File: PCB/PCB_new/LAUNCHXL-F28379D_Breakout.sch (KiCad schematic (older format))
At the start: 25 parts, among them IC1 LM358N, Q1 220mA/50V/3.5Ω, Q10 100V/17A, Q2 100V/17A, Q6 100V/17A, Q7 100V/17A, Q8 100V/17A, Q9 100V/17A

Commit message: updated schematic and packages (need to verify many packages)
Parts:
- removed BRAKE_CONN: 1X2-3.5MM, Drivetrain_control:1X2-3.5MM, symbol PCB_2020-rescue:1X2-3.5MM-Drivetrain_control-eagle-import-Board_Schematic_11201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
- removed D1: 1N4004, Drivetrain_control:DO41-10, symbol PCB_2020-rescue:1N4004-Drivetrain_control-eagle-import-Board_Schematic_112019-r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
- removed unit 2 of DCDC_CONN_12V
- removed unit 2 of IC1
- removed unit 2 of JETSON_CONN_PWR
- removed unit 3 of JETSON_CONN_PWR
- removed MC_CONN: 22-23-2041, Drivetrain_control:22-23-2041, symbol PCB_2020-rescue:22-23-2041-Drivetrain_control-eagle-import-Board_Schematic_1120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
- removed Q10, Q6, Q7, Q8, Q9: 100V/17A, Drivetrain_control:TO220V, symbol PCB_2020-rescue:MOSFET-NCH-FQP30N06L-Drivetrain_control-eagle-import-Board_Sche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
- removed R9: R-US_R0805, Drivetrain_control:R0805, symbol PCB_2020-rescue:R-US_R0805-Drivetrain_control-eagle-import-Board_Schematic_1120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
- removed SERVO_CONN: 5566-8, Drivetrain_control:5566-8, symbol PCB_2020-rescue:5566-8-Drivetrain_control-eagle-import-Board_Schematic_112019-r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
- added J?: SERVO_CONN, symbol Connector:Conn_01x08_Male
- added J?: MC_CONN, Connector_Molex:Molex_Mini-Fit_Jr_5566-04A2_2x02_P4.20mm_Vertical, symbol Connector:Conn_01x04_Male
- added Q? (x4): 100V/17A, Package_TO_SOT_THT:TO-251-3_Vertical, symbol Device:Q_NMOS_DGS
- C1: symbol PCB_2020-rescue:C-Drivetrain_control-eagle-import-Board_Schematic_112019-rescue-PCB_2020-rescue-PCB_2020-rescue -> Device:C
- DCDC_CONN_12V: footprint Drivetrain_control:22-23-2021 -> Connector_Molex:Molex_CLIK-Mate_502382-0270_1x02-1MP_P1.25mm_Vertical; symbol PCB_2020-rescue:22-23-2021-Drivetrain_control-eagle-import-Board_Schematic_112019-rescue-PCB_2020-rescue-PCB_2020-rescue -> Connector:Conn_01x02_Male
- FTDI: symbol PCB_2020-rescue:CONN_06LONGPADS-Drivetrain_control-eagle-import-Board_Schematic_112019-rescue-PCB_2020-rescue-PCB_2020-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 -> PCB_2020:CONN_06LONGPADS-Drivetrain_control
- IC1: footprint Drivetrain_control:DIL08 -> Package_DIP:DIP-8_W10.16mm; symbol PCB_2020-rescue:LM358N-Drivetrain_control-eagle-import-Board_Schematic_112019-rescue-PCB_2020-rescue-PCB_2020-rescue -> Amplifier_Operational:LM358
- JETSON_CONN_PWR: footprint Drivetrain_control:22-23-2031 -> Connector_Molex:Molex_CLIK-Mate_502382-0370_1x03-1MP_P1.25mm_Vertical; symbol PCB_2020-rescue:22-23-2031-Drivetrain_control-eagle-import-Board_Schematic_112019-rescue-PCB_2020-rescue-PCB_2020-rescue -> Connector:Conn_01x03_Male
- Q1: footprint Drivetrain_control:SOT23-3 -> Package_TO_SOT_THT:TO-251-3_Vertical; symbol PCB_2020-rescue:MOSFET-NCH-BSS138-Drivetrain_control-eagle-import-Board_Schematic_112019-rescue-PCB_2020-rescue-PCB_202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 -> Device:Q_NMOS_DGS
- Q2: footprint Drivetrain_control:TO220V -> Package_TO_SOT_THT:TO-251-3_Vertical; symbol PCB_2020-rescue:MOSFET-NCH-FQP30N06L-Drivetrain_control-eagle-import-Board_Schematic_112019-rescue-PCB_2020-rescue-PCB_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 -> Device:Q_NMOS_DGS
- R1, R18, R2, R3, R4, R5: symbol PCB_2020-rescue:R-US_R0805-Drivetrain_control-eagle-import-Board_Schematic_112019-rescue-PCB_2020-rescue-PCB_2020-rescue -> Device:R
- R16, R17: footprint Drivetrain_control:R0805 -> Resistor_SMD:R_0805_2012Metric_Pad1.15x1.40mm_HandSolder; symbol PCB_2020-rescue:R-US_R0805-Drivetrain_control-eagle-import-Board_Schematic_112019-rescue-PCB_2020-rescue-PCB_2020-rescue -> Device:R
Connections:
- net +12V: now also DCDC_CONN_12V.2 (Pin_2), R18.1, R2.1, R5.1; no longer DCDC_CONN_12V.1 (S), IC1.8 (V+), R18.2, R2.2, R5.2
- net +3V3: now also JETSON_CONN_PWR.2 (Pin_2), Q1.2 (G), R1.1; no longer Q1.1 (G), R1.2
- net +5V: now also JETSON_CONN_PWR.3 (Pin_3); no longer JETSON_CONN_PWR.1 (S)
- net EN+: now also R5.2, J?.5 (Pin_5), Q?.1 (D); no longer R5.1
- net EN+_CTL: now also Q?.2 (G)
- net FS1_CTL: now also Q?.2 (G)
- net FS1_MC: now also J?.4 (Pin_4), Q?.1 (D)
- net FWD_CTL: now also Q?.2 (G)
- net FWD_MC: now also J?.3 (Pin_3), Q?.1 (D)
- net GND: now also DCDC_CONN_12V.1 (Pin_1), JETSON_CONN_PWR.1 (Pin_1), R17.2, R3.2, J?.1 (Pin_1), J?.2 (Pin_2), J?.3 (Pin_3), J?.4 (Pin_4), Q?.3 (S), Q?.3 (S), Q?.3 (S), Q?.3 (S); no longer IC1.4 (V-), R17.1, R3.1
- net HLFB+: now also R16.1, J?.8 (Pin_8); no longer R16.2
- net INPUT_A+: now also Q2.1 (D), R18.2, J?.6 (Pin_6); no longer Q2.2 (D), R18.1
- net INPUT_A+_CTL: now also Q2.2 (G); no longer Q2.1 (G)
- net INPUT_B+: now also Q1.1 (D), R2.2, J?.7 (Pin_7); no longer Q1.3 (D), R2.1
- net MC_HLFB+: now also R16.2, R17.1; no longer R16.1, R17.2
- net REV_CTL: now also Q?.2 (G)
- net REV_MC: now also J?.2 (Pin_2), Q?.1 (D)
- net THROTTLE_DAC: now also IC1.3 (+)
- net THROTTLE_MC: now also IC1.1, R4.2, J?.1 (Pin_1); no longer R4.1
- net TI_PWM: now also Q1.3 (S), R1.2; no longer Q1.2 (S), R1.1
- new net: IC1.2 (-), R3.1, R4.1
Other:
- note added: "Check to make sure that the mollex connection is correct for these!!"
- note added: "Info from past connector\nDrivetrain_control:22-23-2041\nPCB_2020-rescue:22-23-2041-Drivetrain_control-eagle-import"
- note added: "check size of molex connector"
- note added: "check this mollex connector too!!"
- note added: "find out what happened to the ground Vdd pins\n"

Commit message: cleaned up breakout and headers files
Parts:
- IC1: symbol Amplifier_Operational:LM358 -> PCB_2020:LM358_with_power_pins
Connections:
- net +12V: now also IC1.5
- net GND: now also IC1.4
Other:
- note removed: "find out what happened to the ground Vdd pins\n"
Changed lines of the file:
@@
 EESchema Schematic File Version 4
+LIBS:PCB_2020-cache
 EELAYER 30 0
 EELAYER END
@@
 encoding utf-8
 Sheet 3 3
-Title ""
-Date ""
+Title "AMP Breakout"
+Date "2019-12-13"
 Rev ""
 Comp ""
@@
 Wire Wire Line
 	3100 3800 3100 4000
-Text GLabel 2600 3800 2    70   BiDi ~ 0
-GND
-Wire Wire Line
-	4600 3800 4600 3900
 Wire Wire Line
 	4600 3900 5300 3900
@@
 	7400 1500 7200 1500
 Wire Wire Line
-	2300 1500 2300 1600
-Wire Wire Line
-	2300 1600 2300 1700
-Wire Wire Line
-	2300 1700 2300 1800
-Wire Wire Line
-	3000 1600 2300 1600
-Text GLabel 2700 1500 2    70   BiDi ~ 0
-GND
-Text GLabel 2700 1600 2    70   BiDi ~ 0
-GND
-Connection ~ 2300 1600
-Text GLabel 2700 1700 2    70   BiDi ~ 0
-GND
-Connection ~ 2300 1700
-Text GLabel 2700 1800 2    70   BiDi ~ 0
-GND
-Connection ~ 2300 1800
-Wire Wire Line
 	7800 3400 7800 3500
 Wire Wire Line
 	10300 1700 10200 1700
 Wire Wire Line
-	4900 3500 5100 3500
-Wire Wire Line
 	5100 3500 5100 4100
 Wire Wire Line
 	5100 3500 5600 3500
-Connection ~ 5100 3500
 Text Label 5450 3500 0    70   ~ 0
 THROTTLE_MC
-Text Label 10950 4650 2    70   ~ 0
+Text Label 10950 4650 2    39   ~ 0
 THROTTLE_MC
 Wire Wire Line
 	4300 3600 4300 4100
 Connection ~ 4300 4100
-Wire Wire Line
-	4300 3400 4100 3400
-Text GLabel 4100 3400 0    70   BiDi ~ 0
+Text GLabel 4100 3400 0    39   BiDi ~ 0
 THROTTLE_DAC
 Wire Wire Line
 	2000 3400 2600 3400
-Text GLabel 2600 3400 2    70   BiDi ~ 0
+Text GLabel 2600 3400 2    39   BiDi ~ 0
 SCIB_RX
 Wire Wire Line
 	2000 3500 2600 3500
-Text GLabel 2600 3500 2    70   BiDi ~ 0
+Text GLabel 2600 3500 2    39   BiDi ~ 0
 SCIB_TX
 Wire Wire Line
@@
 Wire Wire Line
 	3100 3600 3100 3000
-Text GLabel 2600 3600 2    70   BiDi ~ 0
-+3V3
 Wire Wire Line
 	4800 1300 4800 1100
@@
 Wire Wire Line
 	9800 1600 9800 1300
-Wire Wire Line
-	4600 3200 4600 2900
 Wire Wire Line
 	4600 2900 4600 2700
@@
 Wire Wire Line
 	3000 1400 2900 1400
-Text Label 2900 1400 2    70   ~ 0
+Text Label 2900 1400 2    39   ~ 0
 EN+
 Wire Wire Line
@@
 Wire Wire Line
 	3000 1300 2900 1300
-Text Label 2900 1300 2    70   ~ 0
+Text Label 2900 1300 2    39   ~ 0
 INPUT_A+
 Wire Wire Line
@@
 Wire Wire Line
 	1900 1100 1900 1400
-Text Label 1900 1100 0    70   ~ 0
+Text Label 1900 1100 0    39   ~ 0
 HLFB+
 Wire Wire Line
@@
 Text Label 11100 2900 0    70   ~ 0
 FS1_MC
-Text Label 10950 4350 2    70   ~ 0
+Text Label 10950 4350 2    39   ~ 0
 FS1_MC
 Wire Wire Line
@@
 Text Label 8900 2900 0    70   ~ 0
 REV_MC
-Text Label 10950 4550 2    70   ~ 0
+Text Label 10950 4550 2    39   ~ 0
 REV_MC
 Text Label 4500 1700 2    70   ~ 0
@@
 Wire Wire Line
 	10200 1500 10200 1300
-Text GLabel 8600 3200 3    70   BiDi ~ 0
+Text GLabel 8600 3200 3    39   BiDi ~ 0
 REV_CTL
-Text GLabel 6400 3200 3    70   BiDi ~ 0
+Text GLabel 6400 3200 3    39   BiDi ~ 0
 EN+_CTL
-Text GLabel 9700 3200 3    70   BiDi ~ 0
+Text GLabel 9700 3200 3    39   BiDi ~ 0
 FWD_CTL
-Text GLabel 10800 3200 3    70   BiDi ~ 0
+Text GLabel 10800 3200 3    39   BiDi ~ 0
 FS1_CTL
-Text GLabel 1900 1800 0    70   BiDi ~ 0
+Text GLabel 1900 1800 0    39   BiDi ~ 0
 MC_HLFB+
-Text GLabel 7500 3200 3    70   BiDi ~ 0
+Text GLabel 7500 3200 3    39   BiDi ~ 0
 INPUT_A+_CTL
 $Comp
@@
 $EndComp
 $Comp
-L Amplifier_Operational:LM358 IC1
+L PCB_2020:LM358_with_power_pins IC1
 U 1 1 70C115B9
-P 4600 3500
+P 4650 3500
 AR Path="/70C115B9" Ref="IC1"  Part="3"
 AR Path="/5DD5E236/70C115B9" Ref="IC1"  Part="3"
 AR Path="/5DF27AC1/70C115B9" Ref="IC1"  Part="1"
-F 0 "IC1" H 4700 3625 59  0001 L BNN
-F 1 "LM358N" H 4700 3300 59  0001 L BNN
-F 2 "Package_DIP:DIP-8_W10.16mm" H 4600 3500 50  0001 C CNN
-F 3 "" H 4600 3500 50  0001 C CNN
-	1    4600 3500
+F 0 "IC1" H 4750 3625 59  0001 L BNN
+F 1 "LM358N" H 4750 3300 59  0001 L BNN
+F 2 "Package_DIP:DIP-8_W10.16mm" H 4650 3500 50  0001 C CNN
+F 3 "" H 4650 3500 50  0001 C CNN
+	1    4650 3500
 	1    0    0    -1
 $EndComp
@@
 L power:GND #GND16
 U 1 1 4CC6CA08
-P 2300 2100
+P 2650 2100
 AR Path="/4CC6CA08" Ref="#GND16"  Part="1"
 AR Path="/5DD5E236/4CC6CA08" Ref="#GND16"  Part="1"
 AR Path="/5DF27AC1/4CC6CA08" Ref="#GND16"  Part="1"
-F 0 "#GND16" H 2300 2100 50  0001 C CNN
-F 1 "GND" H 2200 1900 59  0000 L BNN
-F 2 "" H 2300 2100 50  0001 C CNN
-F 3 "" H 2300 2100 50  0001 C CNN
-	1    2300 2100
+F 0 "#GND16" H 2650 2100 50  0001 C CNN
+F 1 "GND" H 2550 1900 59  0000 L BNN
+F 2 "" H 2650 2100 50  0001 C CNN
+F 3 "" H 2650 2100 50  0001 C CNN
+	1    2650 2100
 	1    0    0    -1
 $EndComp
@@
 Text Notes 7200 900  0    59   ~ 0
 12V supply comes from DC-DC Converter\nwhich supplies 13.8 nominal and 12V @ peak current
-Wire Wire Line
-	2300 1500 3000 1500
 Text GLabel 4800 1700 3    50   Input ~ 0
 TI_PWM
@@
 Wire Wire Line
 	1900 2250 1900 2500
-Wire Wire Line
-	2300 1800 2300 2100
-Text Label 2900 1200 2    70   ~ 0
+Text Label 2900 1200 2    39   ~ 0
 INPUT_B+
 $Comp
@@
 Text Notes 2250 750  0    50   ~ 10
 check size of molex connector
-Wire Wire Line
-	3000 1800 2300 1800
-Wire Wire Line
-	3000 1700 2300 1700
 $Comp
 L Connector:Conn_01x08_Male J?
@@
 Text Notes 10900 4950 0    50   ~ 10
 Info from past connector\nDrivetrain_control:22-23-2041\nPCB_2020-rescue:22-23-2041-Drivetrain_control-eagle-import
-Text Label 10950 4450 2    70   ~ 0
+Text Label 10950 4450 2    39   ~ 0
 FWD_MC
 Wire Wire Line
@@
 Wire Wire Line
 	5300 3250 5300 3900
-Text Notes 4100 2900 0    50   ~ 10
-find out what happened to the ground Vdd pins\n
+Wire Wire Line
+	4100 3400 4350 3400
+Wire Wire Line
+	4300 3600 4350 3600
+Wire Wire Line
+	4600 3750 4600 3900
+Wire Wire Line
+	4600 2900 4600 3250
+Wire Wire Line
+	4950 3500 5100 3500
+Connection ~ 5100 3500
+Wire Wire Line
+	2650 1500 2650 1600
+Wire Wire Line
+	3000 1500 2650 1500
+Wire Wire Line
+	3000 1600 2650 1600
+Connection ~ 2650 1600
+Wire Wire Line
+	2650 1600 2650 1700
+Wire Wire Line
+	3000 1700 2650 1700
+Connection ~ 2650 1700
+Wire Wire Line
+	3000 1800 2650 1800
+Wire Wire Line
+	2650 1700 2650 1800
+Connection ~ 2650 1800
+Wire Wire Line
+	2650 1800 2650 2100
 $EndSCHEMATC

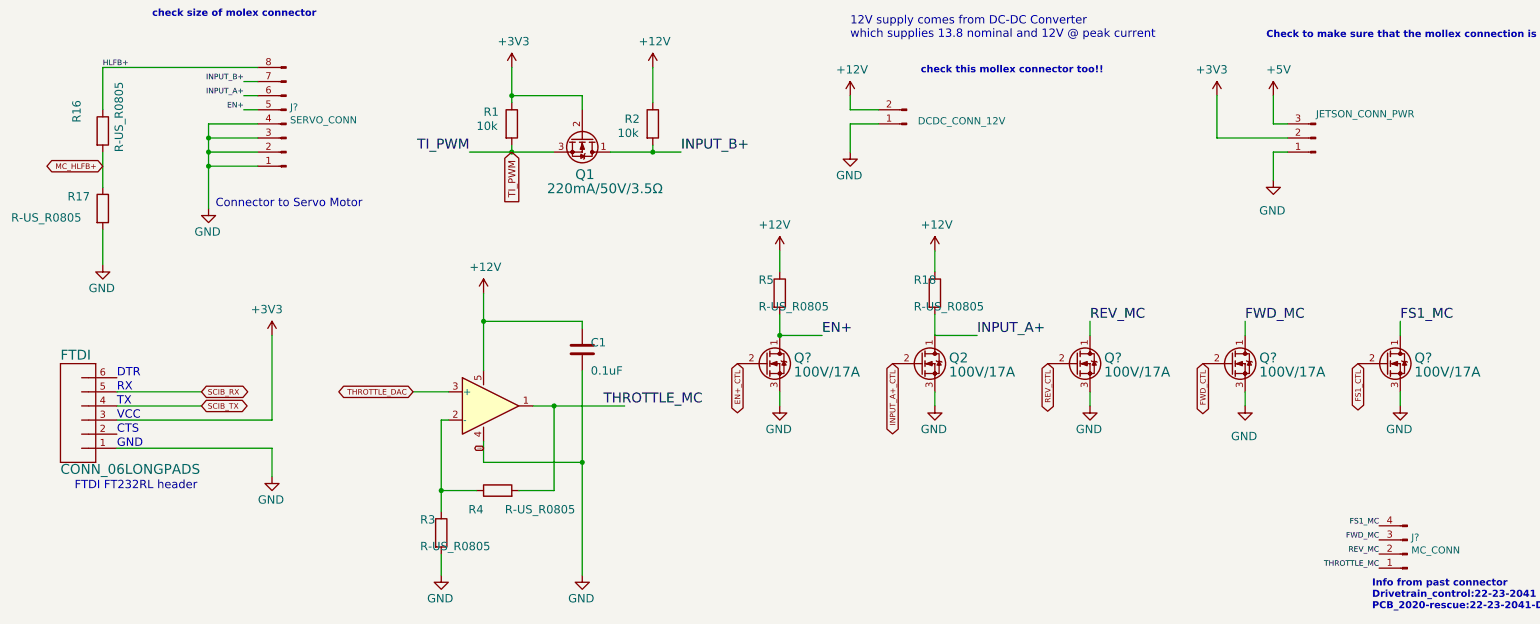
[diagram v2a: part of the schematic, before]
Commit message: added no connection indicators
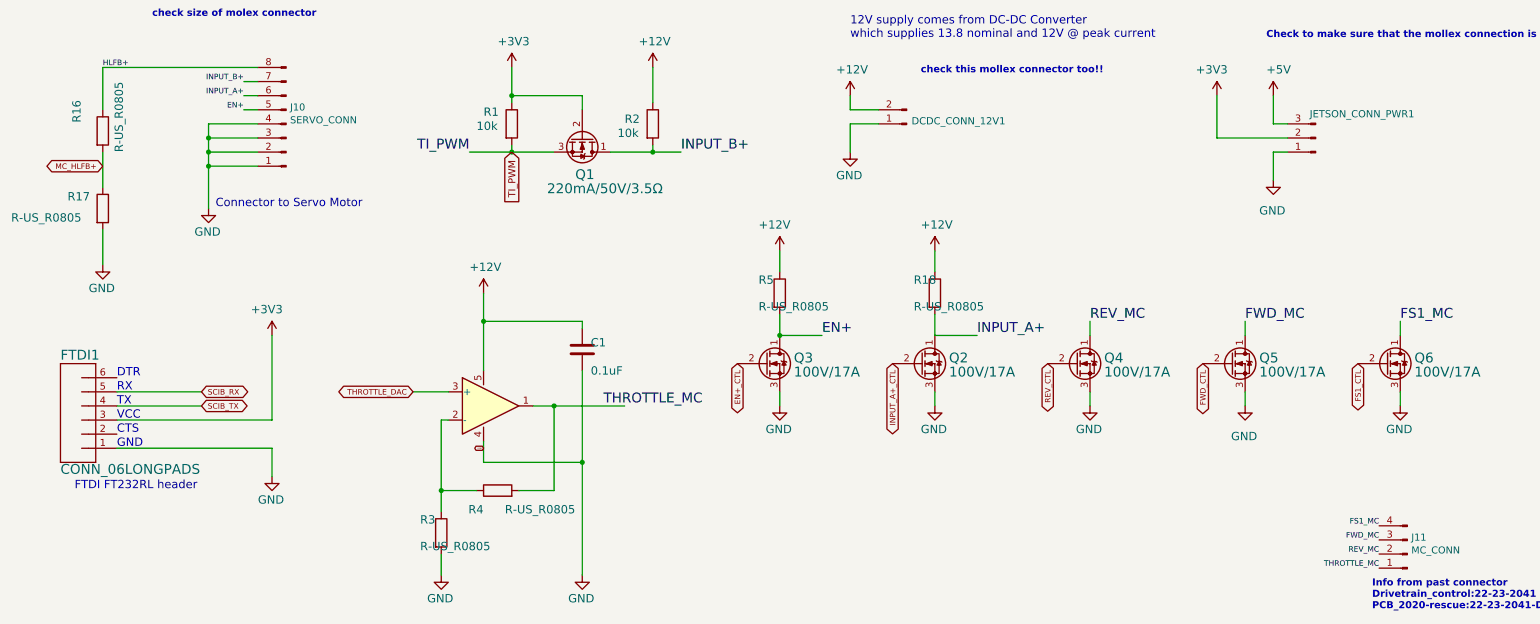
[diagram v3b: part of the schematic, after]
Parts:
- gave numbers to parts that had none: 6
